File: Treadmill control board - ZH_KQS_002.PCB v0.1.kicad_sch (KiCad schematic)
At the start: 31 parts, among them CN1_V_H Conn_01x04_Pin, Q1 S8050, Q7 IRG4PC40U, U1 L7812CV, U2 L7805

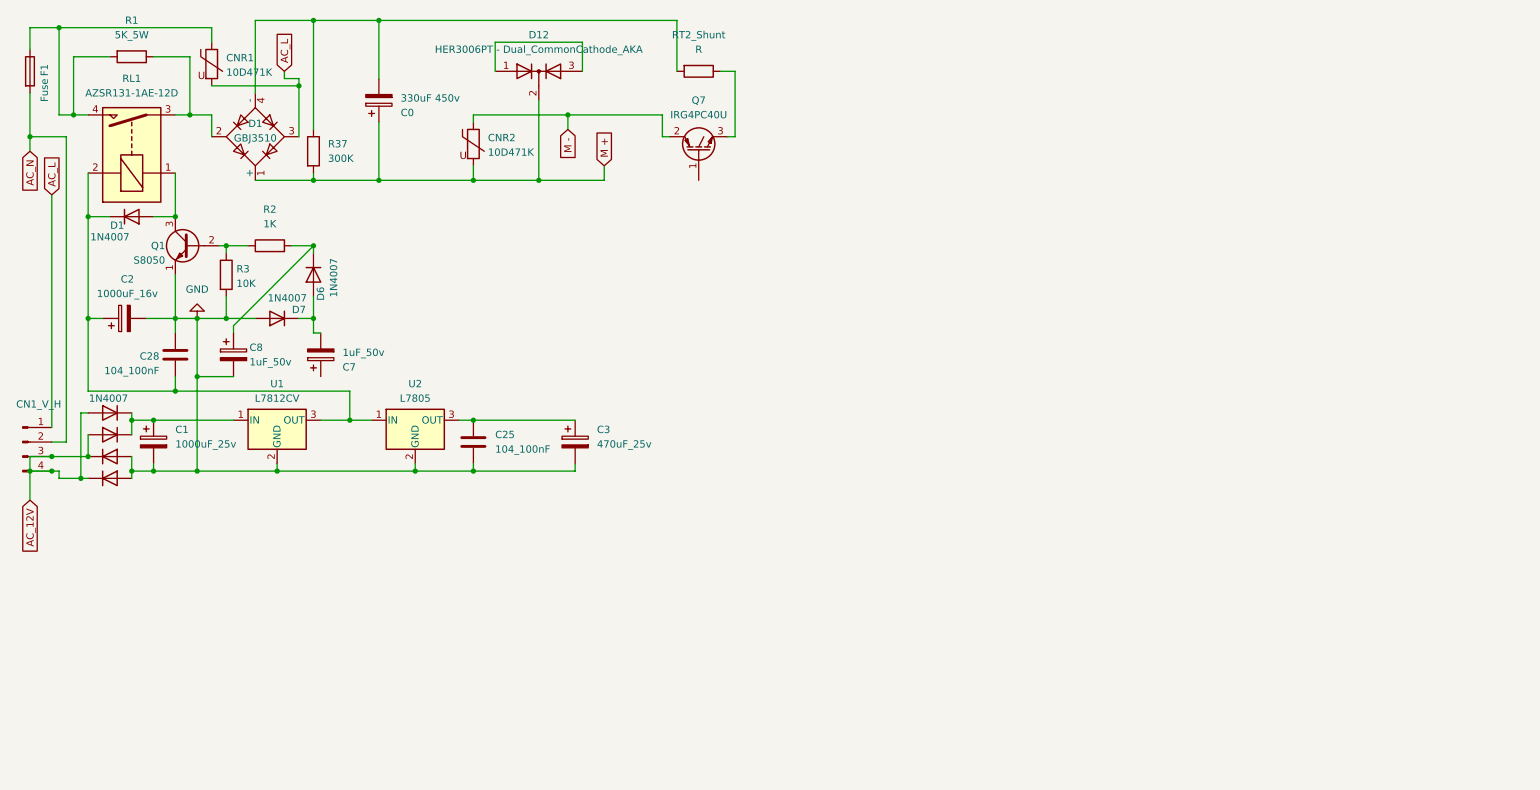
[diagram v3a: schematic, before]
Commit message: Added OpAmp stages, CPU socket
Added the operational amplifier stages and CPU Socket, rearrange of power supply Rails
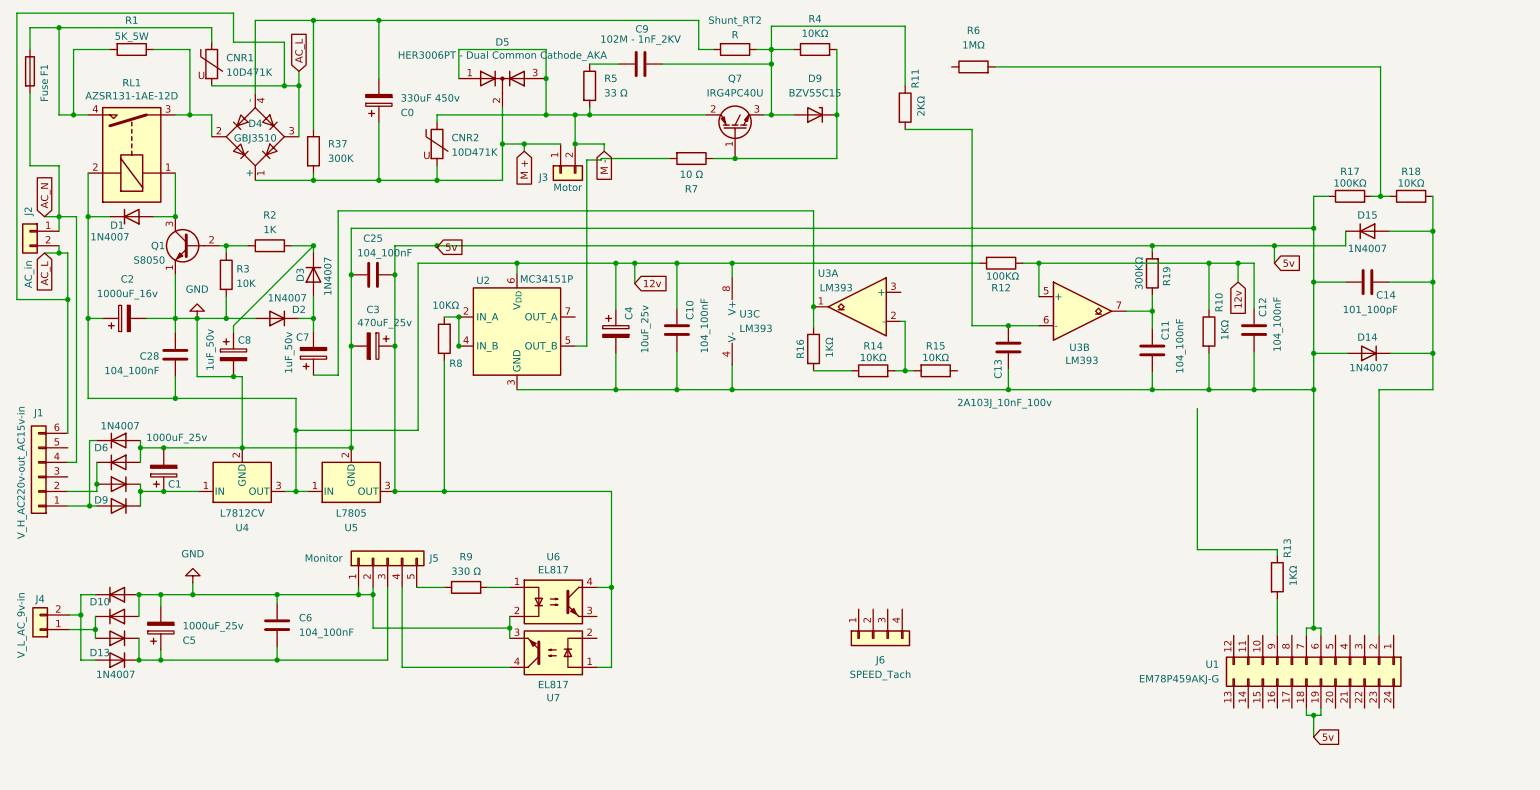
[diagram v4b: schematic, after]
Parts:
- removed CN1_V_H: Conn_01x04_Pin, Connector_JST:JST_VH_B4P-VH_1x04_P3.96mm_Vertical, symbol Connector:Conn_01x04_Pin
- added C10, C11, C12, C6: 104_100nF, Capacitor_THT:C_Disc_D4.7mm_W2.5mm_P5.00mm, symbol Device:C
- added C13: 2A103J_10nF_100v, Capacitor_THT:C_Rect_L7.0mm_W2.5mm_P5.00mm, symbol Device:C
- added C14: 101_100pF, Capacitor_THT:C_Disc_D4.7mm_W2.5mm_P5.00mm, symbol Device:C
- added C4: 10uF_25v, Capacitor_THT:CP_Radial_D5.0mm_P2.50mm, symbol Device:C_Polarized
- added C5: 1000uF_25v, Capacitor_THT:CP_Radial_D8.0mm_P3.80mm, symbol Device:C_Polarized
- added C9: 102M - 1nF_2KV, Capacitor_THT:C_Disc_D6.0mm_W2.5mm_P5.00mm, symbol Device:C
- added D10, D11, D12, D13, D14, D15: 1N4007, Diode_THT:D_DO-41_SOD81_P10.16mm_Horizontal, symbol Diode:1N4007
- added D9: BZV55C15, Diode_SMD:D_SOD-523, symbol Diode:BZV55C15
- added J1: V_H_AC220v-out_AC15v-in, Connector_JST:JST_VH_B6P-VH_1x06_P3.96mm_Vertical, symbol Connector_Generic:Conn_01x06
- added J2: AC_in, Connector_Wire:SolderWire-1.5sqmm_1x02_P6mm_D1.7mm_OD3mm_Relief, symbol Connector_Generic:Conn_01x02
- added J3: Motor, Connector_Wire:SolderWire-1.5sqmm_1x02_P6mm_D1.7mm_OD3mm_Relief, symbol Connector_Generic:Conn_01x02
- added J4: V_L_AC_9v-in, Connector_JST:JST_VH_B2P-VH-B_1x02_P3.96mm_Vertical, symbol Connector_Generic:Conn_01x02
- added J5: Monitor, Connector_JST:JST_XA_B05B-XASK-1_1x05_P2.50mm_Vertical, symbol Connector_Generic:Conn_01x05
- added J6: SPEED_Tach, Connector_JST:JST_XA_B04B-XASK-1_1x04_P2.50mm_Vertical, symbol Connector_Generic:Conn_01x04
- added R10, R13, R16: 1KΩ, Resistor_THT:R_Axial_DIN0207_L6.3mm_D2.5mm_P10.16mm_Horizontal, symbol Device:R
- added R11: 2KΩ, Resistor_THT:R_Axial_DIN0207_L6.3mm_D2.5mm_P10.16mm_Horizontal, symbol Device:R
- added R12, R17: 100KΩ, Resistor_THT:R_Axial_DIN0207_L6.3mm_D2.5mm_P10.16mm_Horizontal, symbol Device:R
- added R14, R15, R18, R4, R8: 10KΩ, Resistor_THT:R_Axial_DIN0207_L6.3mm_D2.5mm_P10.16mm_Horizontal, symbol Device:R
- added R19: 300KΩ, Resistor_THT:R_Axial_DIN0207_L6.3mm_D2.5mm_P10.16mm_Horizontal, symbol Device:R
- added R5: 33 Ω, Resistor_THT:R_Axial_DIN0309_L9.0mm_D3.2mm_P12.70mm_Horizontal, symbol Device:R
- added R6: 1MΩ, Resistor_THT:R_Axial_DIN0411_L9.9mm_D3.6mm_P15.24mm_Horizontal, symbol Device:R
- added R7: 10 Ω, Resistor_THT:R_Axial_DIN0207_L6.3mm_D2.5mm_P10.16mm_Horizontal, symbol Device:R
- added R9: 330 Ω, Resistor_THT:R_Axial_DIN0207_L6.3mm_D2.5mm_P10.16mm_Horizontal, symbol Device:R
- added U1: EM78P459AKJ-G, Package_DIP:DIP-24_W7.62mm_Socket, symbol Connector_Generic:Conn_02x12_Counter_Clockwise
- added U2: MC34151P, Package_DIP:DIP-8_W7.62mm, symbol Driver_FET:MC3x152
- added U3: LM393, Package_DIP:DIP-8_W7.62mm, symbol Comparator:LM393
- added U6, U7: EL817, Package_DIP:DIP-4_W7.62mm, symbol Isolator:EL817
- C0: footprint (none) -> Capacitor_THT:CP_Radial_D35.0mm_P10.00mm_SnapIn
- C1: footprint (none) -> Capacitor_THT:CP_Radial_D8.0mm_P3.80mm
- C25, C28: footprint (none) -> Capacitor_THT:C_Disc_D4.7mm_W2.5mm_P5.00mm
- CNR2: footprint Varistor:RV_Disc_D21.5mm_W6.1mm_P7.5mm -> Varistor:RV_Disc_D9mm_W4.1mm_P5mm
- D5: renamed from D12; value HER3006PT - Dual_CommonCathode_AKA -> HER3006PT - Dual Common Cathode_AKA
- Shunt_RT2: renamed from RT2_Shunt; footprint (none) -> Resistor_THT:R_Bare_Metal_Element_L16.3mm_W4.8mm_P15.30mm
- renumbered D7 to D2, D6 to D3, D1 to D4, D2 to D6, D3 to D7, D4 to D8, D5 to D9, U1 to U4, U2 to U5
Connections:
- net AC_L: now also J1.6 (Pin_6), J2.2 (Pin_2)
- net AC_N: now also J1.4 (Pin_4), J2.1 (Pin_1)
- net GND: now also C25.1, D6.2 (A), D7.2 (A), C10.2, C11.2, C12.2, C13.1, C14.2, C4.2, C5.2, C6.1, D10.2 (A), D11.2 (A), D14.2 (A), J5.1 (Pin_1), J5.2 (Pin_2), R10.2, R17.1, U1.6 (Pin_6), U1.7 (Pin_7), U2.3 (GND), U3.4 (V-), U6.2, U7.3; no longer C25.2, D8.2 (A), D9.2 (A)
- net M +: now also J3.1 (Pin_1)
- net M -: now also D5.1 (A), D5.3 (A), J3.2 (Pin_2), R5.2
- net 12v: now reaches C2.1, C28.2, D1.1 (K), RL1.2, U4.3 (OUT), U5.1 (IN)
- net 12v: now also C10.1, C12.1, C4.1, R10.1, R12.1, R12.2, U2.6 (V_{DD}), U3.5 (+), U3.8 (V+)
- net at C1.1, U4.1 (IN): now also D8.1 (K), D9.1 (K); no longer D6.1 (K), D7.1 (K)
- net at Q7.3 (E), Shunt_RT2.1: now also C9.2, D9.2 (A), R11.1, R4.1
- net 5v: now reaches C3.1, U5.3 (OUT)
- net 5v: now also C25.2, D15.1 (K), R19.2, R8.1, U1.18 (Pin_18), U1.19 (Pin_19), U6.4, U7.1; no longer C25.1
- net at C7.1: now also R16.1, U3.1
- net at Q7.1 (G): now also D9.1 (K), R4.2, R7.1
- removed net AC_12V: D6.2 (A), D7.2 (A), D8.1 (K), D9.1 (K)
- new net: R14.2, R15.2, U3.2 (-)
- new net: C14.1, D14.1 (K), D15.2 (A), R18.2, U1.2 (Pin_2)
- new net: D11.1 (K), D12.2 (A), J4.1 (Pin_1)
- new net: D10.1 (K), D13.2 (A), J4.2 (Pin_2)
- new net: C13.2, R11.2, U3.6 (-)
- new net: D6.1 (K), D9.2 (A), J1.1 (Pin_1)
- new net: D7.1 (K), D8.2 (A), J1.2 (Pin_2)
- new net: R17.2, R18.1, R6.2
- new net: C9.1, R5.1
- new net: C5.1, C6.2, D12.1 (K), D13.1 (K), J5.3 (Pin_3)
- new net: J5.4 (Pin_4), U7.4
- new net: R13.2, U1.9 (Pin_9)
- new net: C11.1, R19.1, U3.7
- new net: J5.5 (Pin_5), R9.1
- new net: R9.2, U6.1
- new net: R14.1, R16.2
- new net: R8.2, U2.2 (IN_A), U2.4 (IN_B)
- new net: R7.2, U2.5 (OUT_B)
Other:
- title: (none) -> Dobrin_Ivanov - Treadmill control board - ZH_KQS_002.PCB
- moved on the sheet: C1, C25, C3, C7, CNR2, D5, Q7, R1, Shunt_RT2, U4, U5

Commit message: Added TX, RX to Monitor and Speed sensor Resistors
Added TX, RX resistors to optrons Monitor connector and CPU and Speed sensor Resistors to connector
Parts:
- added C15: 102_1nF, Capacitor_THT:C_Disc_D4.7mm_W2.5mm_P5.00mm, symbol Device:C
- added C16: 471_470pF, Capacitor_THT:C_Disc_D4.7mm_W2.5mm_P5.00mm, symbol Device:C
- added C17: 104_100nF, Capacitor_THT:C_Disc_D4.7mm_W2.5mm_P5.00mm, symbol Device:C
- added R20: 20 KΩ, Resistor_THT:R_Axial_DIN0207_L6.3mm_D2.5mm_P10.16mm_Horizontal, symbol Device:R
- added R21: 300 Ω, Resistor_THT:R_Axial_DIN0207_L6.3mm_D2.5mm_P10.16mm_Horizontal, symbol Device:R
- added R22, R23: 1 KΩ, Resistor_THT:R_Axial_DIN0207_L6.3mm_D2.5mm_P10.16mm_Horizontal, symbol Device:R
- added R24: 330 Ω, Resistor_THT:R_Axial_DIN0207_L6.3mm_D2.5mm_P10.16mm_Horizontal, symbol Device:R
- J1: value V_H_AC220v-out_AC15v-in -> AC15v-in / V_H_AC220v-out_to_Transformer
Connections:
- net 5v is gone; now on net +5v: C25.2, C3.1, D15.1 (K), R19.2, R8.1, U1.18 (Pin_18), U1.19 (Pin_19), U5.3 (OUT), U6.4, U7.1
- net 12v: no longer C10.1, C2.1, C28.2, C4.1, D1.1 (K), R12.2, RL1.2, U2.6 (V_{DD}), U3.8 (V+), U4.3 (OUT), U5.1 (IN)
- net GND: now also R15.1, C15.1, R22.2
- net M -: now also R6.1
- net at J6.1 (Pin_1): now also C17.2, R21.1
- net at J6.2 (Pin_2): now also J6.3 (Pin_3), J6.4 (Pin_4), C16.1, C17.1
- net at U7.2: now also R24.2
- net at U1.16 (Pin_16): now also R23.2
- net at U1.17 (Pin_17): now also R24.1
- net at U1.9 (Pin_9): now also R13.1; no longer R13.2
- net +5v: now reaches R14.1, R16.2
- net +5v: now also R20.1, R21.2
- net at U3.3 (+): now also R13.2
- net at U6.3: now also C15.2, R22.1, R23.1
- new net: C16.2, R20.2
- new net +12v: C10.1, C2.1, C28.2, C4.1, D1.1 (K), R12.2, RL1.2, U2.6 (V_{DD}), U3.8 (V+), U4.3 (OUT), U5.1 (IN)
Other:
- moved on the sheet: C12, C13, J6, R10, R11, R12, R13, R14, R15, R16, R6, U1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

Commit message: Refactored Power Rails, added resistors and other components between OpAmps, Speed sensor and CPU
Refactored Power Rails, added resistors and other components between OpAmps, Speed sensor and CPU
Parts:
- added C18: 101_100pF, Capacitor_THT:C_Disc_D4.7mm_W2.5mm_P5.00mm, symbol Device:C
- added D16: BZV55C6V8, Diode_THT:D_DO-35_SOD27_P10.16mm_Horizontal, symbol Diode:BZV55C6V8
- added D17, D18: 1N4007, Diode_THT:D_DO-41_SOD81_P10.16mm_Horizontal, symbol Diode:1N4007
- added Q2: S8050, Package_TO_SOT_THT:TO-92_Inline, symbol Transistor_BJT:S8050
- added R25: 2 KΩ, Resistor_THT:R_Axial_DIN0207_L6.3mm_D2.5mm_P10.16mm_Horizontal, symbol Device:R
- added R26, R27, R29, R31: 10 KΩ, Resistor_THT:R_Axial_DIN0207_L6.3mm_D2.5mm_P10.16mm_Horizontal, symbol Device:R
- added R28: 20 KΩ, Resistor_THT:R_Axial_DIN0207_L6.3mm_D2.5mm_P10.16mm_Horizontal, symbol Device:R
- added R30: 1 KΩ, Resistor_THT:R_Axial_DIN0207_L6.3mm_D2.5mm_P10.16mm_Horizontal, symbol Device:R
- D9: footprint Diode_SMD:D_SOD-523 -> Diode_THT:D_DO-35_SOD27_P10.16mm_Horizontal
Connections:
- net +12v: now also D16.1 (K)
- net +5v: now also U1.14 (Pin_14), D17.1 (K), R31.2
- net GND: now also C16.2, C17.1, J6.2 (Pin_2), J6.3 (Pin_3), C18.2, D18.2 (A), Q2.1 (E), R26.1, R27.1, R29.1
- net at U1.10 (Pin_10): now also R28.1
- net at U1.11 (Pin_11): now also R26.2
- net at U1.12 (Pin_12): now also R27.2
- net at U1.13 (Pin_13): now also C18.1, R30.2
- net at U1.15 (Pin_15): now also R8.2, U2.2 (IN_A), U2.4 (IN_B)
- net at U1.8 (Pin_8): now also R25.2
- net at C11.1, R19.1, U3.7: now also R25.1
- net at R20.2: now also C16.1, J6.4 (Pin_4), Q2.2 (B); no longer C16.2
- new net: D17.2 (A), D18.1 (K), Q2.3 (C), R30.1, R31.1
- new net: D16.2 (A), R28.2, R29.2
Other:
- moved on the sheet: C11, C12, C13, C14, C15, C16, C25, C3, D14, D15, J6, R10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

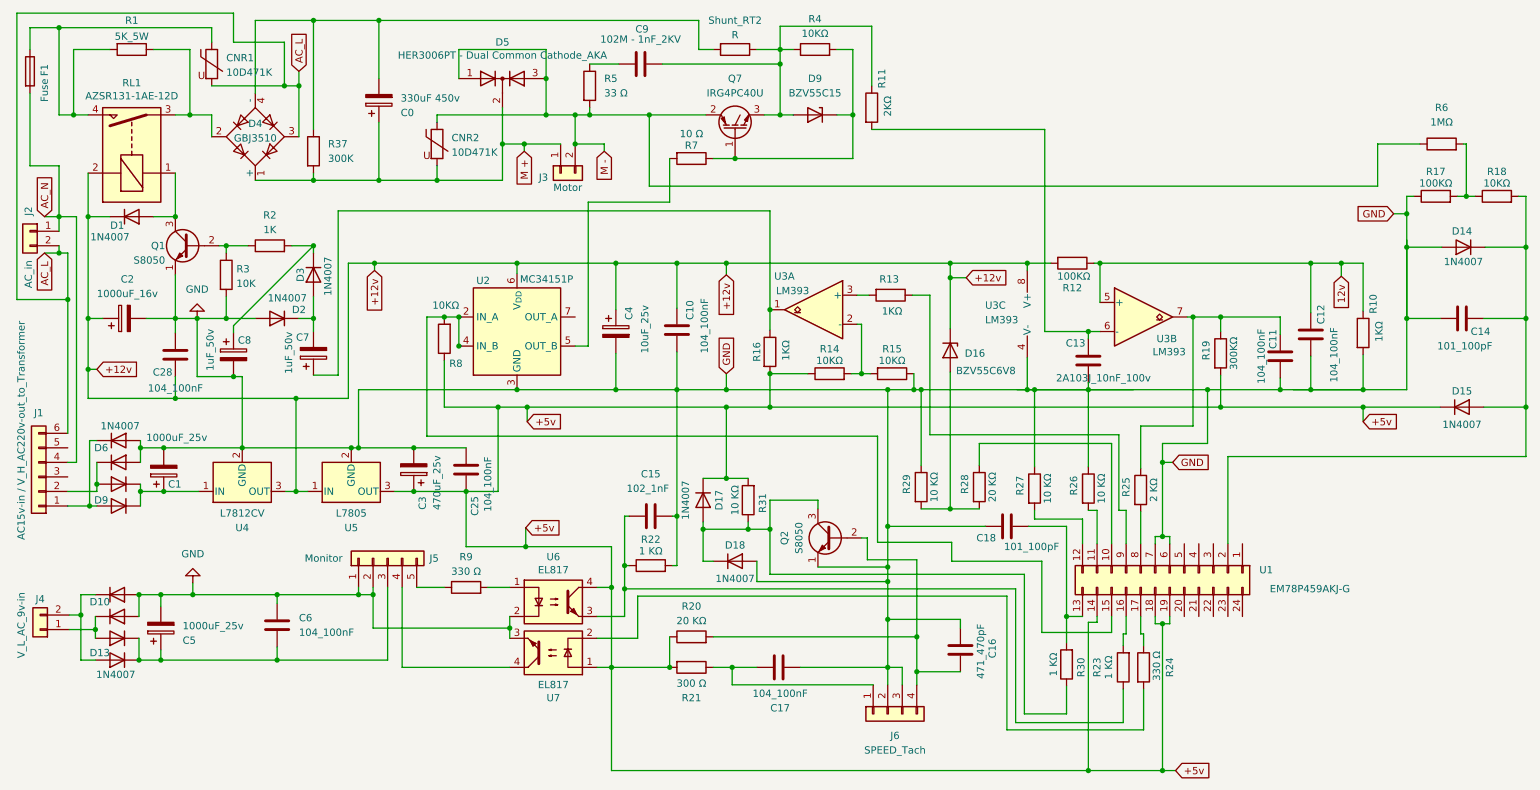
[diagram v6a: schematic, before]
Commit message: Final, Added Shunt Resistor value, Crystal Oscillator and accompanying resistors
Final, Added Shunt Resistor value, Crystal Oscillator and accompanying resistors
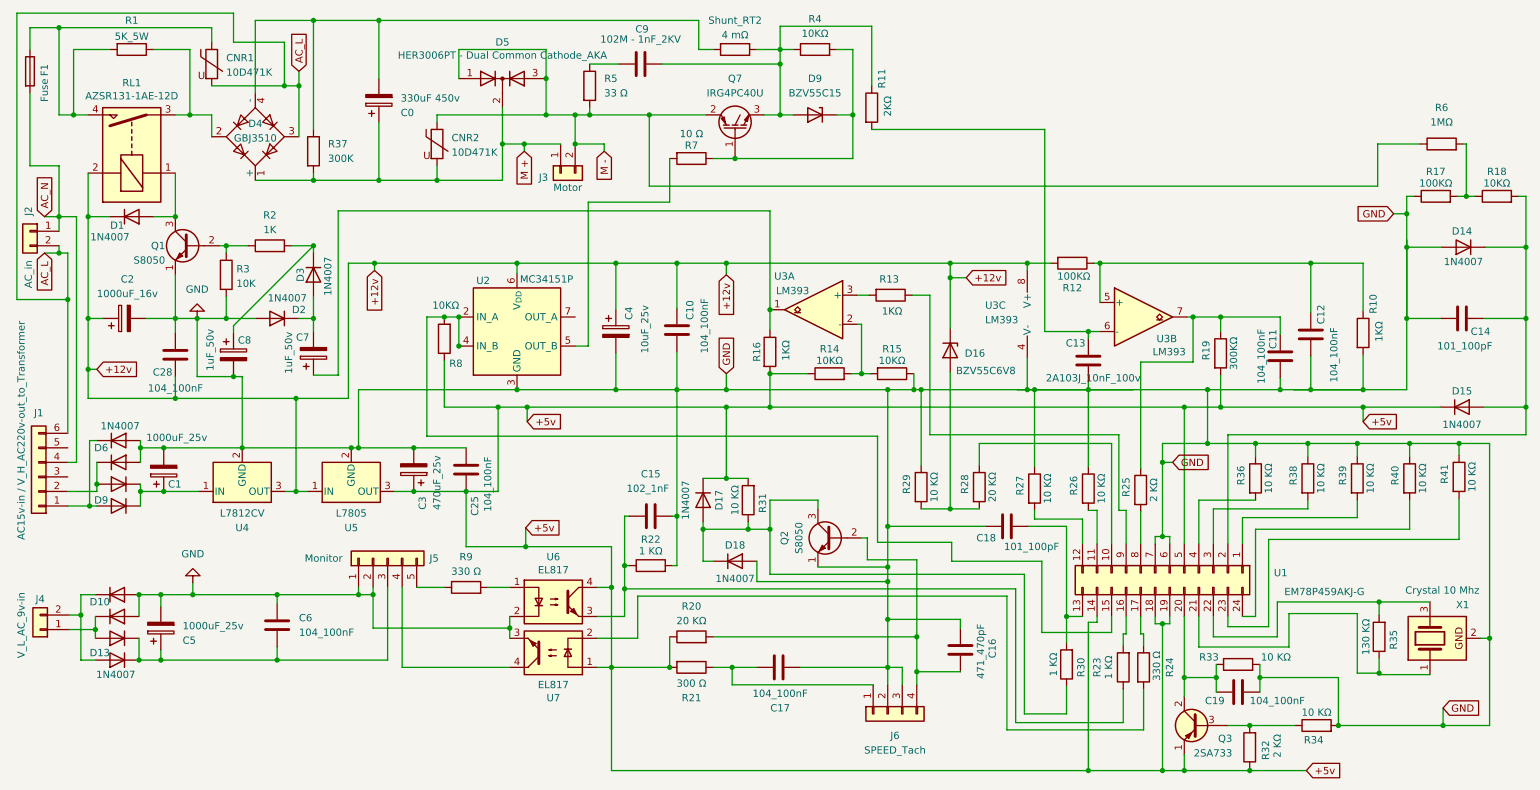
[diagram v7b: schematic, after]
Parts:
- added C19: 104_100nF, Capacitor_THT:C_Disc_D4.7mm_W2.5mm_P5.00mm, symbol Device:C
- added Q3: 2SA733, PCM_Package_TO_SOT_THT_AKL:TO-92_Inline_Wide_ECB, symbol PCM_Transistor_BJT_AKL:2SA733
- added R32: 2 KΩ, Resistor_THT:R_Axial_DIN0207_L6.3mm_D2.5mm_P10.16mm_Horizontal, symbol Device:R
- added R33, R34, R36, R38, R39, R40, R41: 10 KΩ, Resistor_THT:R_Axial_DIN0207_L6.3mm_D2.5mm_P10.16mm_Horizontal, symbol Device:R
- added R35: 130 KΩ, Resistor_THT:R_Axial_DIN0207_L6.3mm_D2.5mm_P10.16mm_Horizontal, symbol Device:R
- added X1: Crystal 10 Mhz, Crystal:Crystal_HC49-U-3Pin_Vertical, symbol PCM_Crystal_AKL:Crystal_Generic_GND2
- Shunt_RT2: value R -> 4 mΩ
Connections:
- net +5v: now also U1.5 (Pin_5), Q3.1 (E), R32.1
- net GND: now also C19.1, R33.2, R34.2, R36.1, R38.1, R39.1, R40.1, R41.1, X1.2
- net at U1.1 (Pin_1): now also R39.2
- net at U1.20 (Pin_20): now also C19.2, Q3.2 (C), R33.1
- net at U1.21 (Pin_21): now also R35.1, X1.1
- net at U1.22 (Pin_22): now also R35.2, X1.3
- net at U1.23 (Pin_23): now also R41.2
- net at U1.24 (Pin_24): now also R40.2
- net at U1.3 (Pin_3): now also R38.2
- net at U1.4 (Pin_4): now also R36.2
- net 12v: no longer names the net of C12.1, R10.1, R12.1, U3.5 (+)
- new net: Q3.3 (B), R32.2, R34.1
